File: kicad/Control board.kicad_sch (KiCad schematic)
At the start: 15 parts, among them J1 ESP32-C3 Supermini, J2 Rotary, J3 TFT Display (0.96"), J4 PTC Starter, K1 JQC-3FF-S-Z

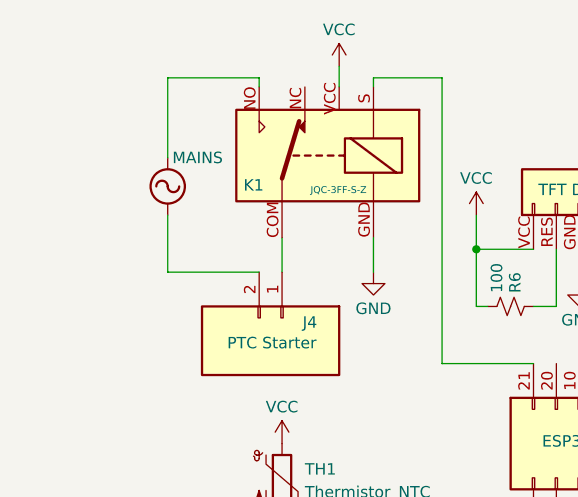
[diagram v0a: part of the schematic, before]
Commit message: added USB charger to the overall circuit to clarify power feed
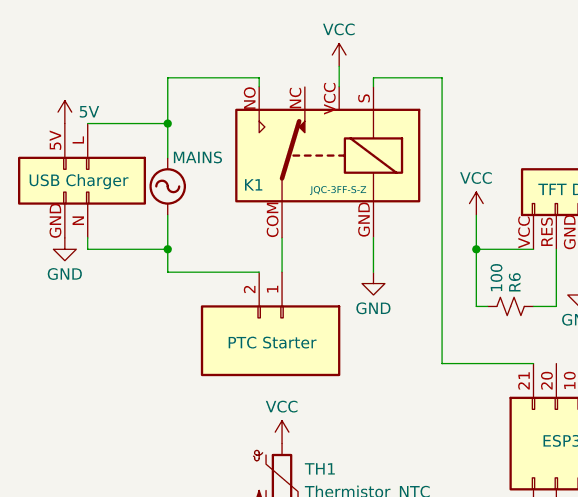
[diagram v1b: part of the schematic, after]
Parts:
- added J5: USB Charger, symbol Connector_Generic:Conn_02x02_Odd_Even
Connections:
- net 5V: now also J5.5V (Pin_3)
- net GND: now also J5.GND (Pin_4)
- net MAINS: now also J5.N (Pin_2)
- net at K1.NO: now also J5.L (Pin_1)

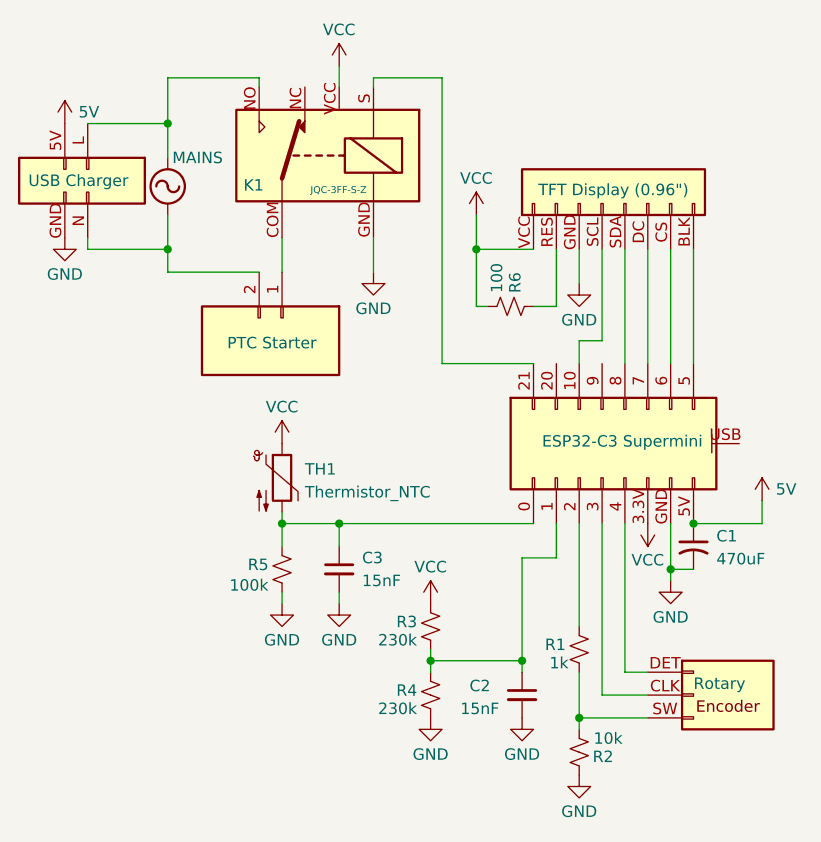
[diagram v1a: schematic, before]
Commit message: moved capacitor to relay power pin
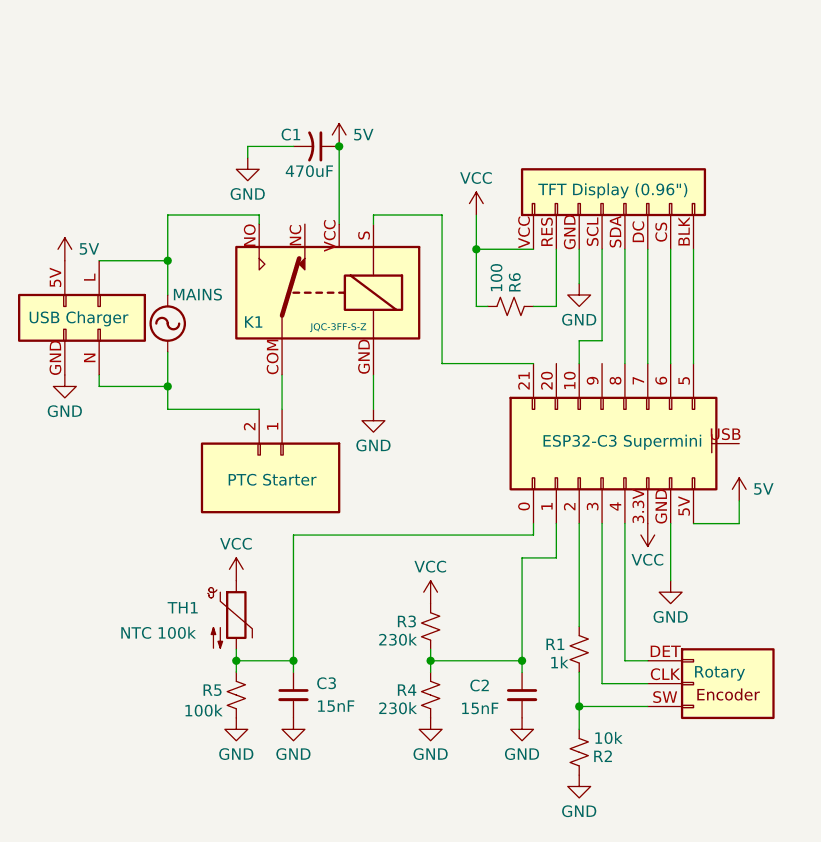
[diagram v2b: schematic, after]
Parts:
- TH1: value Thermistor_NTC -> NTC 100k
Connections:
- net 5V: now also K1.VCC
- net VCC: no longer K1.VCC
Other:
- moved on the sheet: C1, C3, K1, R5, TH1
